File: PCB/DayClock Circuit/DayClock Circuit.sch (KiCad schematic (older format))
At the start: 7 parts, among them J1 Servo Conn_01x03_Male, J2 LED Strip Conn_01x03_Male, J3 5V Power Connector, J4 Input Button Connector, U1 Tiny_RTC_DS1307

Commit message: Added 2004 LCD screen connector to schematic
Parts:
- added J5: 4002 LCD Screen, Connectors_JST:JST_XH_B04B-XH-A_04x2.50mm_Straight, symbol Connector_Generic:Conn_01x04_Male
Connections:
- net labels added: SCL, SDA
- net labels removed: RTC_SCL, RTC_SDA
- wire segments 20 -> 22
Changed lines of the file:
@@
-$EndComp
-$Comp
-L power:GND #PWR07
-U 1 1 5A79654F
-P 8000 4225
-F 0 "#PWR07" H 8000 3975 50  0001 C CNN
-F 1 "GND" H 8005 4052 50  0000 C CNN
-F 2 "" H 8000 4225 50  0001 C CNN
-F 3 "" H 8000 4225 50  0001 C CNN
-	1    8000 4225
-	1    0    0    -1
 $EndComp
 $Comp
@@
 Wire Wire Line
 	5450 2875 5800 2875
-Text Label 3475 3575 0    50   ~ 0
-RTC_SCL
-Text Label 3475 3675 0    50   ~ 0
-RTC_SDA
+Text Label 7800 4975 0    50   ~ 0
+SCL
+Text Label 7800 5075 0    50   ~ 0
+SDA
 Wire Wire Line
-	3475 3575 3800 3575
+	7800 4975 7975 4975
 Wire Wire Line
-	3475 3675 3800 3675
+	7800 5075 7975 5075
 $Comp
 L power:+5V #PWR09
@@
 	3800 3775 3275 3775
 Text Label 6900 3375 0    50   ~ 0
-RTC_SCL
+SCL
 Text Label 6900 3275 0    50   ~ 0
-RTC_SDA
+SDA
 Wire Wire Line
 	6800 3375 6900 3375
@@
 Text Label 6800 2875 0    50   ~ 0
 BTN_3
+$Comp
+L Connector_Generic:Conn_01x04_Male J5
+U 1 1 5AFFD786
+P 8175 5175
+F 0 "J5" H 7800 5000 50  0000 C CNN
+F 1 "4002 LCD Screen" H 7750 5125 50  0000 C CNN
+F 2 "Connectors_JST:JST_XH_B04B-XH-A_04x2.50mm_Straight" H 8175 5175 50  0001 C CNN
+F 3 "~" H 8175 5175 50  0001 C CNN
+	1    8175 5175
+	-1   0    0    1
+$EndComp
+$Comp
+L power:+5V #PWR?
+U 1 1 5AFFEF10
+P 7650 5175
+F 0 "#PWR?" H 7650 5025 50  0001 C CNN
+F 1 "+5V" H 7665 5348 50  0000 C CNN
+F 2 "" H 7650 5175 50  0001 C CNN
+F 3 "" H 7650 5175 50  0001 C CNN
+	1    7650 5175
+	1    0    0    -1
+$EndComp
+$Comp
+L power:GND #PWR?
+U 1 1 5AFFEF2B
+P 7650 5275
+F 0 "#PWR?" H 7650 5025 50  0001 C CNN
+F 1 "GND" H 7655 5102 50  0000 C CNN
+F 2 "" H 7650 5275 50  0001 C CNN
+F 3 "" H 7650 5275 50  0001 C CNN
+	1    7650 5275
+	1    0    0    -1
+$EndComp
+Wire Wire Line
+	7975 5275 7650 5275
+Wire Wire Line
+	7650 5175 7975 5175
+$Comp
+L power:GND #PWR?
+U 1 1 5B001950
+P 8000 4225
+F 0 "#PWR?" H 8000 3975 50  0001 C CNN
+F 1 "GND" H 8005 4052 50  0000 C CNN
+F 2 "" H 8000 4225 50  0001 C CNN
+F 3 "" H 8000 4225 50  0001 C CNN
+	1    8000 4225
+	1    0    0    -1
+$EndComp
 $EndSCHEMATC

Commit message: Updated CAD for new TFT screen, and updated schamatic, adding the encoder.
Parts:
- added J6: Encoder, symbol Connector_Generic:Conn_01x05
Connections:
- net labels added: ENC_CLK, ENC_DT, ENC_SW
- wire segments 22 -> 23
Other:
- moved on the sheet: U1
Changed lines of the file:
@@
 L rich_symbols:Tiny_RTC_DS1307 U1
 U 1 1 5A71AFB0
-P 4300 3825
-F 0 "U1" H 4300 4512 60  0000 C CNN
-F 1 "Tiny_RTC_DS1307" H 4300 4406 60  0000 C CNN
-F 2 "rich-footprints:TinyRTC-one-mounting-hole" H 4350 3925 60  0001 C CNN
-F 3 "" H 4350 3925 60  0000 C CNN
-	1    4300 3825
+P 4375 5100
+F 0 "U1" H 4375 5787 60  0000 C CNN
+F 1 "Tiny_RTC_DS1307" H 4375 5681 60  0000 C CNN
+F 2 "rich-footprints:TinyRTC-one-mounting-hole" H 4425 5200 60  0001 C CNN
+F 3 "" H 4425 5200 60  0000 C CNN
+	1    4375 5100
 	1    0    0    -1
 $EndComp
@@
 L power:+5V #PWR09
 U 1 1 5A797DC1
-P 3275 3775
-F 0 "#PWR09" H 3275 3625 50  0001 C CNN
-F 1 "+5V" H 3290 3948 50  0000 C CNN
-F 2 "" H 3275 3775 50  0001 C CNN
-F 3 "" H 3275 3775 50  0001 C CNN
-	1    3275 3775
+P 3350 5050
+F 0 "#PWR09" H 3350 4900 50  0001 C CNN
+F 1 "+5V" H 3365 5223 50  0000 C CNN
+F 2 "" H 3350 5050 50  0001 C CNN
+F 3 "" H 3350 5050 50  0001 C CNN
+	1    3350 5050
 	1    0    0    -1
 $EndComp
@@
 L power:GND #PWR010
 U 1 1 5A797DF4
-P 3800 3875
-F 0 "#PWR010" H 3800 3625 50  0001 C CNN
-F 1 "GND" H 3805 3702 50  0000 C CNN
-F 2 "" H 3800 3875 50  0001 C CNN
-F 3 "" H 3800 3875 50  0001 C CNN
-	1    3800 3875
-	1    0    0    -1
-$EndComp
-Wire Wire Line
-	3800 3775 3275 3775
+P 3875 5150
+F 0 "#PWR010" H 3875 4900 50  0001 C CNN
+F 1 "GND" H 3880 4977 50  0000 C CNN
+F 2 "" H 3875 5150 50  0001 C CNN
+F 3 "" H 3875 5150 50  0001 C CNN
+	1    3875 5150
+	1    0    0    -1
+$EndComp
+Wire Wire Line
+	3875 5050 3350 5050
 Text Label 6900 3375 0    50   ~ 0
 SCL
@@
 L power:GND #PWR013
 U 1 1 5A79A6E1
-P 4450 2750
-F 0 "#PWR013" H 4450 2500 50  0001 C CNN
-F 1 "GND" H 4455 2577 50  0000 C CNN
-F 2 "" H 4450 2750 50  0001 C CNN
-F 3 "" H 4450 2750 50  0001 C CNN
-	1    4450 2750
+P 4500 3875
+F 0 "#PWR013" H 4500 3625 50  0001 C CNN
+F 1 "GND" H 4505 3702 50  0000 C CNN
+F 2 "" H 4500 3875 50  0001 C CNN
+F 3 "" H 4500 3875 50  0001 C CNN
+	1    4500 3875
 	1    0    0    -1
 $EndComp
@@
 	1    0    0    -1
 $EndComp
+$Comp
+L Connector_Generic:Conn_01x05 J6
+U 1 1 5B03D90E
+P 4300 3675
+F 0 "J6" H 4220 3250 50  0000 C CNN
+F 1 "Encoder" H 4220 3341 50  0000 C CNN
+F 2 "" H 4300 3675 50  0001 C CNN
+F 3 "~" H 4300 3675 50  0001 C CNN
+	1    4300 3675
+	-1   0    0    1
+$EndComp
+$Comp
+L power:+5V #PWR?
+U 1 1 5B03DD9C
+P 4950 3775
+F 0 "#PWR?" H 4950 3625 50  0001 C CNN
+F 1 "+5V" H 4965 3948 50  0000 C CNN
+F 2 "" H 4950 3775 50  0001 C CNN
+F 3 "" H 4950 3775 50  0001 C CNN
+	1    4950 3775
+	1    0    0    -1
+$EndComp
+Wire Wire Line
+	4500 3775 4950 3775
+Text Label 6800 3175 0    50   ~ 0
+ENC_SW
+Text Label 4500 3675 0    50   ~ 0
+ENC_SW
+Text Label 4500 3575 0    50   ~ 0
+ENC_DT
+Text Label 4500 3475 0    50   ~ 0
+ENC_CLK
+Text Label 5800 2475 2    50   ~ 0
+ENC_DT
+Text Label 5800 2675 2    50   ~ 0
+ENC_CLK
 $EndSCHEMATC

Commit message: Updated Scheematic to inclide New RGB LED strips and i2c driver,  and 32x64 matrix using an Arduino Uno
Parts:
- removed DS1: TFT-Screen-1.44-SPI-128*128, Socket_Strips:Socket_Strip_Straight_1x08_Pitch2.54mm, symbol rich_symbols:TFT-Screen-1.44-SPI-128*128
- removed J2: LED Strip Conn_01x03_Male, Connectors_JST:JST_XH_B03B-XH-A_03x2.50mm_Straight, symbol Connector_Generic:Conn_01x03_Male
- added A?: Arduino_UNO_R3, Module:Arduino_UNO_R3, symbol MCU_Module:Arduino_UNO_R3
- added J7, J8, J9: RGB_LED_Strip_Connector, symbol rich_symbols:RGB_LED_Strip_Connector
- added J?: Conn_02x08_Odd_Even, symbol Connector_Generic:Conn_02x08_Odd_Even
- added J?: Conn_01x04, symbol Connector_Generic:Conn_01x04
- added Q? (x9): BSP129, Package_TO_SOT_SMD:SOT-223-3_TabPin2, symbol Transistor_FET:BSP129
- added R1, R? (x8): 100k, symbol Device:R
- added U?: PCA9685_i2c_PWM_driver, symbol rich_symbols:PCA9685_i2c_PWM_driver
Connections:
- net labels added: +12V, ST1_BLUE, ST1_GREEN, ST1_RED, ST2_BLUE, ST2_GREEN, ST2_RED, ST3_BLUE, ST3_GREEN, ST3_RED, UNO_A0, UNO_A1, UNO_A2, UNO_A3, UNO_D10, UNO_D2, UNO_D3, UNO_D4, UNO_D5, UNO_D6, UNO_D7, UNO_D8, UNO_D9
- net labels removed: LED_DATA, TFT_A0, TFT_CS, TFT_RST, TFT_SCK, TFT_SDA
- wire segments 23 -> 98
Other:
- note added: "LED Strip 1"
- note added: "LED Strip 2"
- note added: "LED Strip 3"
- note added: "Note: Break out into seperate PCB"
- note added: "i2c LED PWM Driver"
- moved on the sheet: A1, J1, J3, J4, J5, J6, U1

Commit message: Started moving components to the Arduino Mega,  moved the 3 LED strips (9 PWM pins), and the 32x64 Matrix Display
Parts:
- removed A?: Arduino_UNO_R3, Module:Arduino_UNO_R3, symbol MCU_Module:Arduino_UNO_R3
- removed J?: Conn_01x04, symbol Connector_Generic:Conn_01x04
- removed U?: PCA9685_i2c_PWM_driver, symbol rich_symbols:PCA9685_i2c_PWM_driver
- added J11: Conn_01x02, TerminalBlock:TerminalBlock_Altech_AK300-2_P5.00mm, symbol Connector_Generic:Conn_01x02
- added XA1: Arduino_Mega2560_Shield, Arduino:Arduino_Mega2560_Shield, symbol arduino:Arduino_Mega2560_Shield
- J10: renamed from J?; footprint (none) -> Connector_PinHeader_2.54mm:PinHeader_2x08_P2.54mm_Vertical
- J6: footprint (none) -> Connector_JST:JST_XH_B05B-XH-A_1x05_P2.50mm_Vertical
- J7, J8, J9: footprint (none) -> Connector_JST:JST_XH_B04B-XH-A_1x04_P2.50mm_Vertical
- Q1, Q2, Q3, Q4, Q5, Q6, Q7, Q8, Q9: renamed from Q?; value BSP129 -> N-MOSFET
- R1: value 100k -> 10k; footprint (none) -> Resistor_SMD:R_0805_2012Metric_Pad1.15x1.50mm_HandSolder
- R2, R3, R4, R5, R6, R7, R8, R9: renamed from R?; value 100k -> 10k; footprint (none) -> Resistor_SMD:R_0805_2012Metric_Pad1.15x1.50mm_HandSolder
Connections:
- net labels added: A0, A1, A2, A3, D10, D13, D2, D24, D25, D26, D27, D28, D29, D3, D30, D31, D4, D5, D6, D7, D8, D9
- net labels removed: ST1_BLUE, ST1_GREEN, ST1_RED, ST2_BLUE, ST2_GREEN, ST2_RED, ST3_BLUE, ST3_GREEN, ST3_RED, UNO_A0, UNO_A1, UNO_A2, UNO_A3, UNO_D10, UNO_D2, UNO_D3, UNO_D4, UNO_D5, UNO_D6, UNO_D7, UNO_D8, UNO_D9
- wire segments 98 -> 96
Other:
- note added: "32X64 LED Display"
- note added: "WORK IN PROGRESS"
- note removed: "Note: Break out into seperate PCB"
- note removed: "i2c LED PWM Driver"
- moved on the sheet: J10

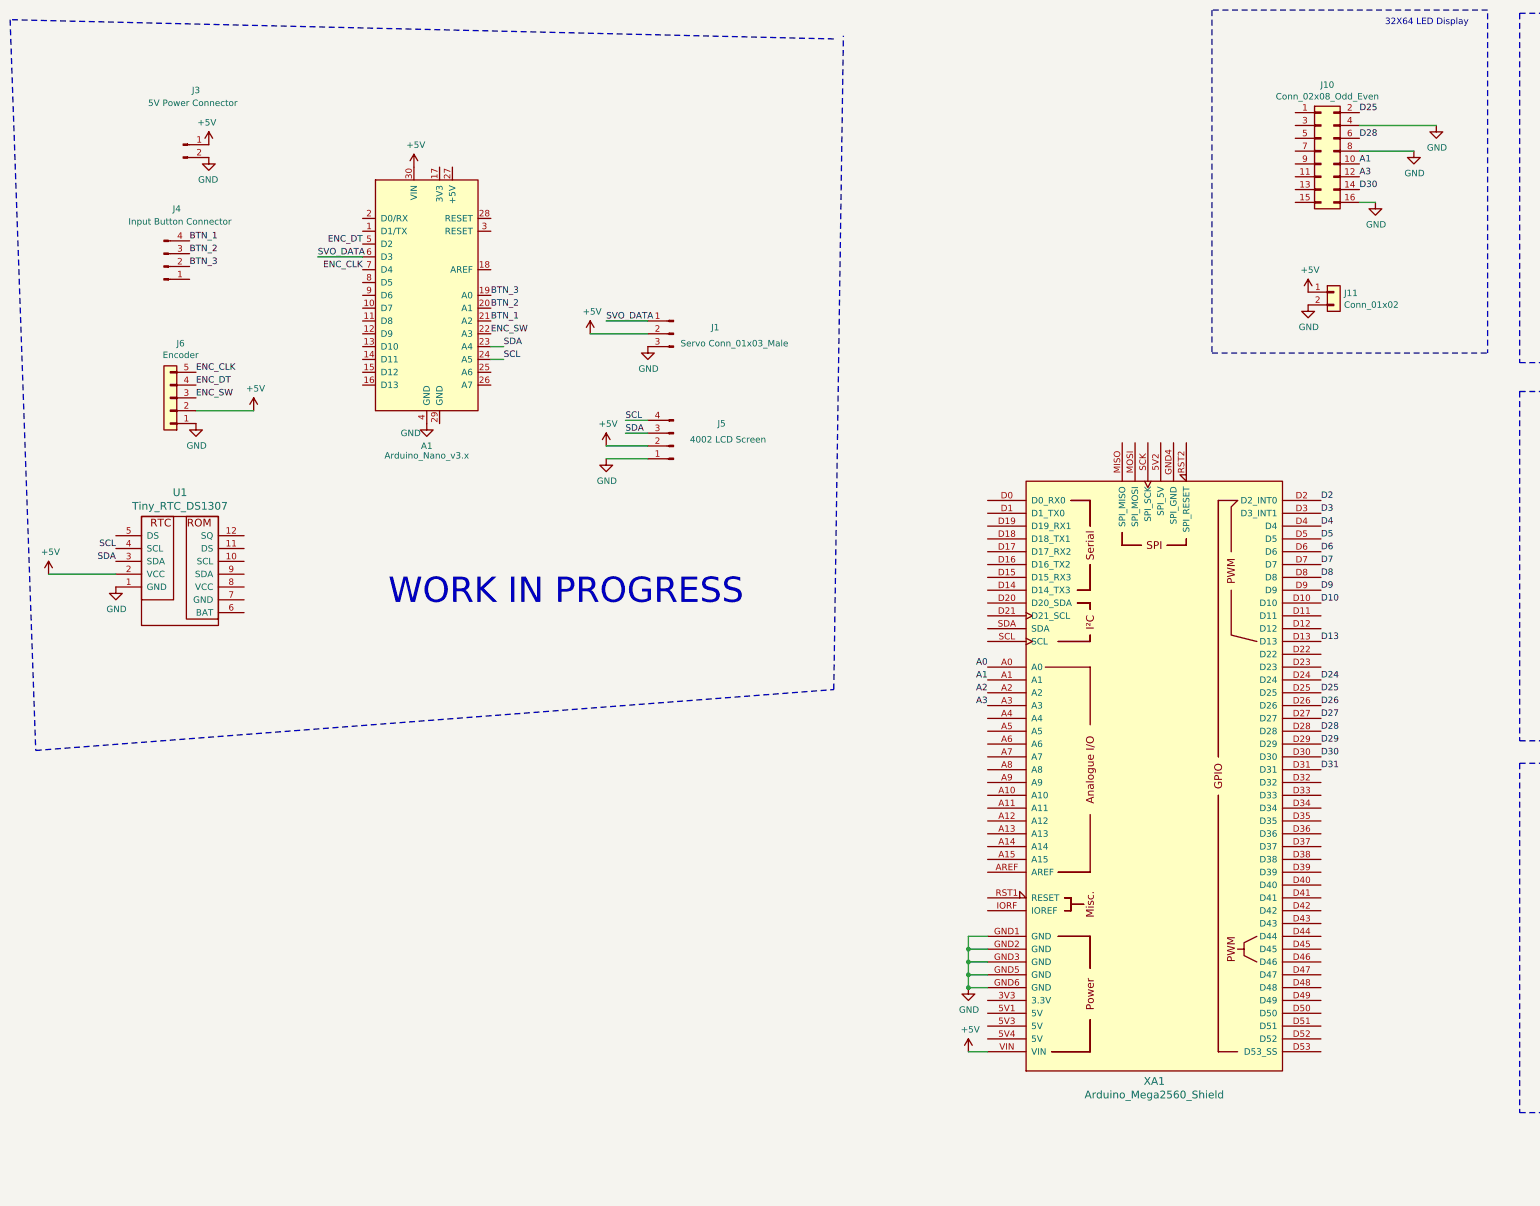
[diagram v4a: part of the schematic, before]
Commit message: Added Power connecter. Moved RTC, Encoder, and 4002 LCD screen to the Arduino Mega.  Lastly need to add stepper, CAT5 breakout for control box, and limit switches for the motor.
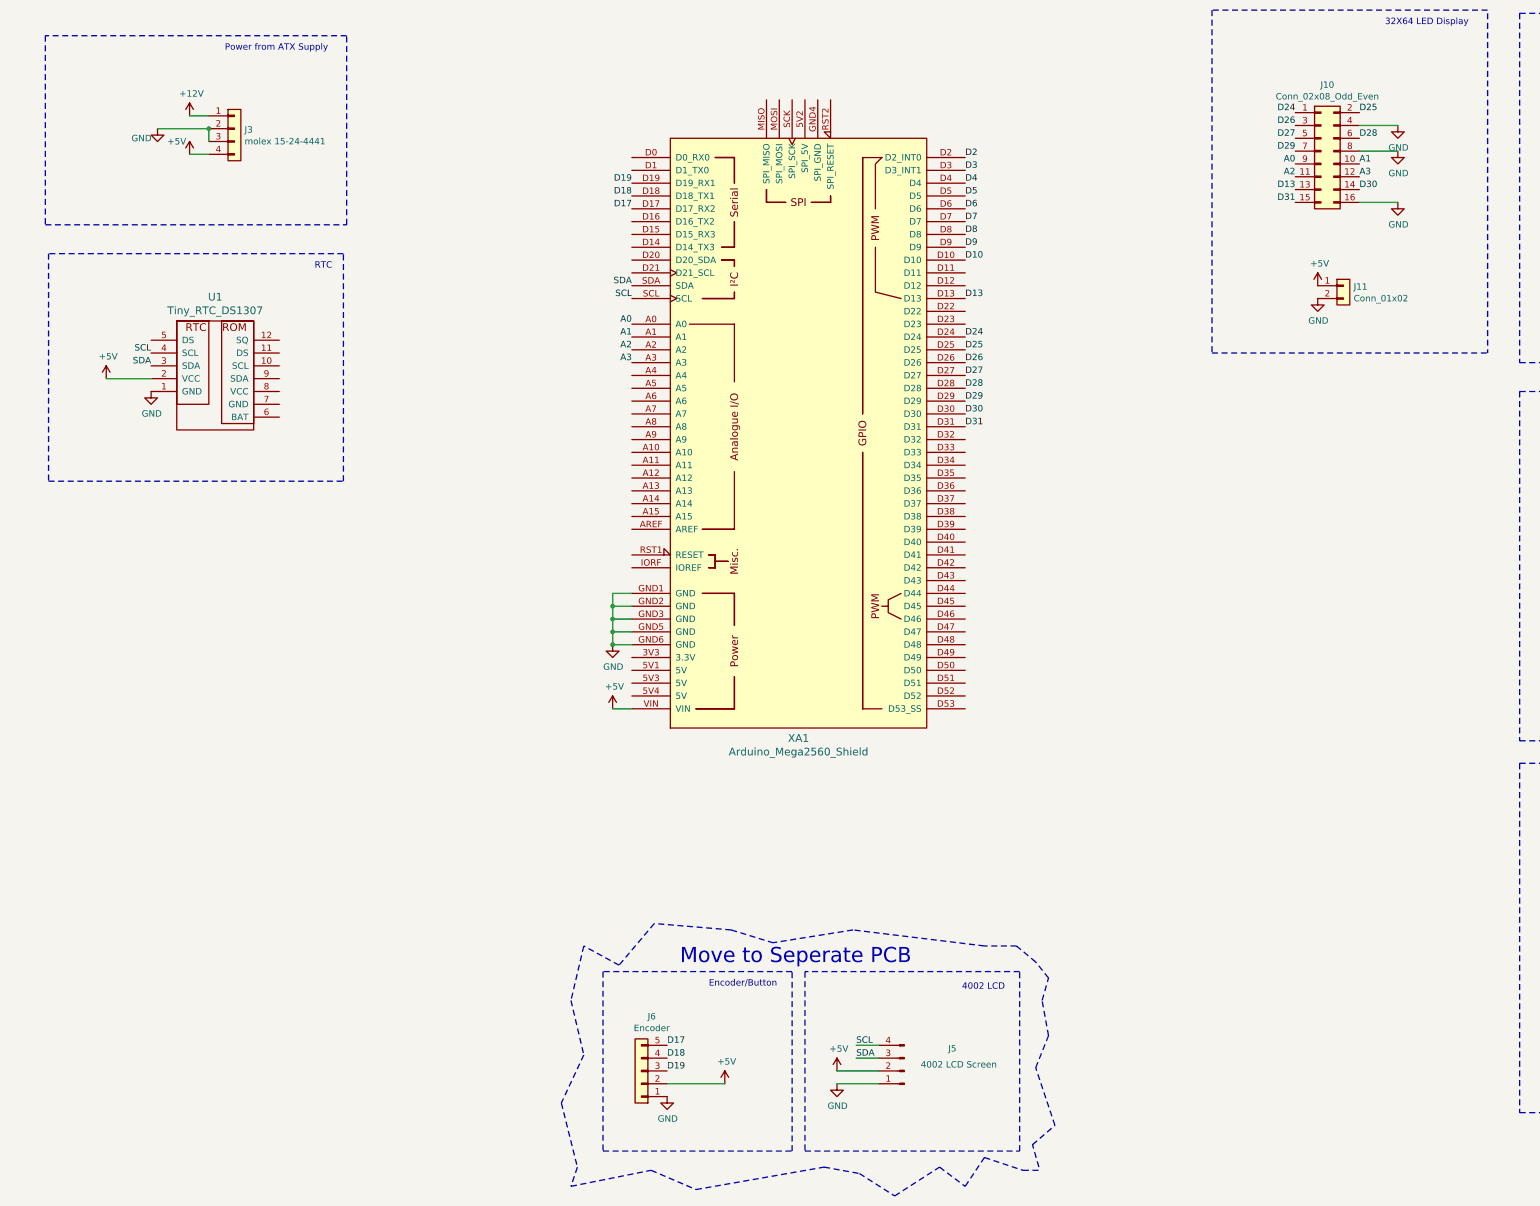
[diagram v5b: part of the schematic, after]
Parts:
- removed A1: Arduino_Nano_v3.x, Modules:Arduino_Nano, symbol MCU_Module:Arduino_Nano_v3.x
- removed J1: Servo Conn_01x03_Male, Connectors_JST:JST_XH_B03B-XH-A_03x2.50mm_Straight, symbol Connector_Generic:Conn_01x03_Male
- removed J3: 5V Power Connector, Connectors_JST:JST_XH_B02B-XH-A_02x2.50mm_Straight, symbol Connector_Generic:Conn_01x02_Male
- removed J4: Input Button Connector, Connectors_JST:JST_XH_B04B-XH-A_04x2.50mm_Straight, symbol Connector_Generic:Conn_01x04_Male
- added J3: molex 15-24-4441, TerminalBlock_Phoenix:TerminalBlock_Phoenix_MKDS-1,5-4-5.08_1x04_P5.08mm_Horizontal, symbol Connector_Generic:Conn_01x04
- Q1, Q2, Q3, Q4, Q5, Q6, Q7, Q8, Q9: footprint Package_TO_SOT_SMD:SOT-223-3_TabPin2 -> Package_TO_SOT_THT:TO-251_IPAK_Vertical
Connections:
- net ENC_CLK is gone; now on net D17: J6.5 (Pin_5)
- net ENC_DT is gone; now on net D18: J6.4 (Pin_4)
- net ENC_SW is gone; now on net D19: J6.3 (Pin_3)
- net +12V: now also J3.1 (Pin_1)
- net +5V: now also J3.4 (Pin_4)
- net A0: now also J10.9 (Pin_9)
- net A2: now also J10.11 (Pin_11)
- net D13: now also J10.13 (Pin_13)
- net D24: now also J10.1 (Pin_1)
- net D26: now also J10.3 (Pin_3)
- net D27: now also J10.5 (Pin_5)
- net D29: now also J10.7 (Pin_7)
- net D31: now also J10.15 (Pin_15)
- net GND: now also J3.2 (Pin_2), J3.3 (Pin_3)
- net SCL: now also XA1.SCL
- net SDA: now also XA1.SDA
- net D17: now reaches XA1.D17 (D17_RX2)
- net D18: now reaches XA1.D18 (D18_TX1)
- net D19: now reaches XA1.D19 (D19_RX1)
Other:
- note added: "4002 LCD"
- note added: "Encoder/Button"
- note added: "Move to Seperate PCB"
- note added: "Power from ATX Supply"
- note added: "RTC"
- note removed: "WORK IN PROGRESS"
- moved on the sheet: J11, J5, J6, U1, XA1
